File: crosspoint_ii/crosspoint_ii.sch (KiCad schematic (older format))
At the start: 1 part, among them P1 DIN_41612_128P

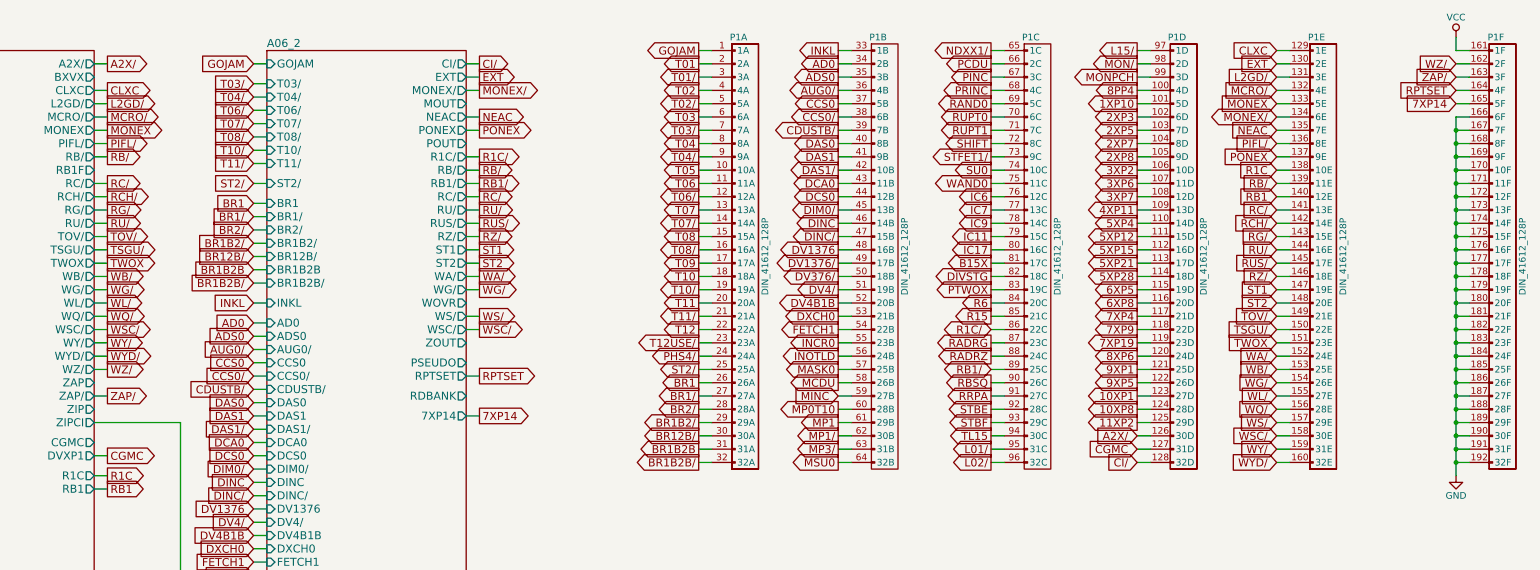
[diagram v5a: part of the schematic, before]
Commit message: Added the final four bit module. All 16 bits of the central/special registers are present. We're stuck at address 0 because TC is using RAD, which needs to be translated into RG or RZ by module 12
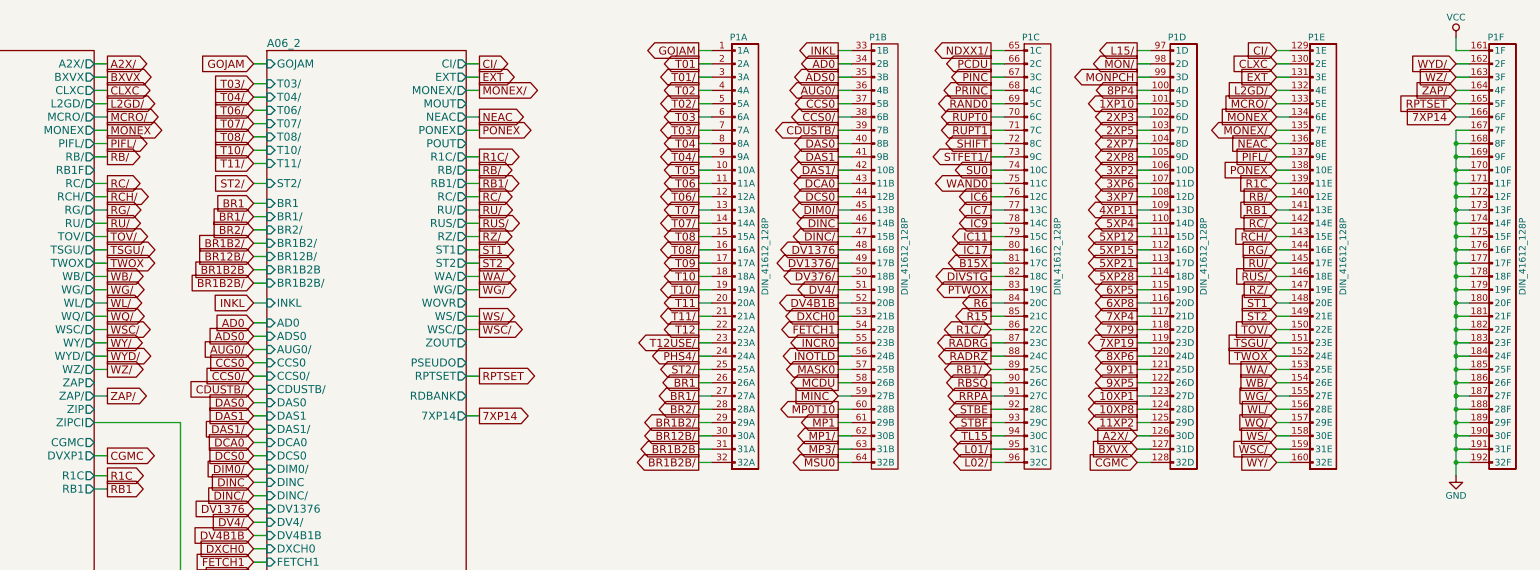
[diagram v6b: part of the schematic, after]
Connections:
- net 7XP14: now also P1.166 (6F); no longer P1.165 (5F)
- net CGMC: now also P1.128 (32D); no longer P1.127 (31D)
- net CI/: now also P1.129 (1E); no longer P1.128 (32D)
- net CLXC: now also P1.130 (2E); no longer P1.129 (1E)
- net EXT: now also P1.131 (3E); no longer P1.130 (2E)
- net GND: no longer P1.166 (6F)
- net L2GD/: now also P1.132 (4E); no longer P1.131 (3E)
- net MCRO/: now also P1.133 (5E); no longer P1.132 (4E)
- net MONEX: now also P1.134 (6E); no longer P1.133 (5E)
- net MONEX/: now also P1.135 (7E); no longer P1.134 (6E)
- net NEAC: now also P1.136 (8E); no longer P1.135 (7E)
- net PIFL/: now also P1.137 (9E); no longer P1.136 (8E)
- net PONEX: now also P1.138 (10E); no longer P1.137 (9E)
- net R1C: now also P1.139 (11E); no longer P1.138 (10E)
- net RB/: now also P1.140 (12E); no longer P1.139 (11E)
- net RB1: now also P1.141 (13E); no longer P1.140 (12E)
- net RC/: now also P1.142 (14E); no longer P1.141 (13E)
- net RCH/: now also P1.143 (15E); no longer P1.142 (14E)
- net RG/: now also P1.144 (16E); no longer P1.143 (15E)
- net RPTSET: now also P1.165 (5F); no longer P1.164 (4F)
- net RU/: now also P1.145 (17E); no longer P1.144 (16E)
- net RUS/: now also P1.146 (18E); no longer P1.145 (17E)
- net RZ/: now also P1.147 (19E); no longer P1.146 (18E)
- net ST1: now also P1.148 (20E); no longer P1.147 (19E)
- net ST2: now also P1.149 (21E); no longer P1.148 (20E)
- net TOV/: now also P1.150 (22E); no longer P1.149 (21E)
- net TSGU/: now also P1.151 (23E); no longer P1.150 (22E)
- net TWOX: now also P1.152 (24E); no longer P1.151 (23E)
- net WA/: now also P1.153 (25E); no longer P1.152 (24E)
- net WB/: now also P1.154 (26E); no longer P1.153 (25E)
- net WG/: now also P1.155 (27E); no longer P1.154 (26E)
- net WL/: now also P1.156 (28E); no longer P1.155 (27E)
- net WQ/: now also P1.157 (29E); no longer P1.156 (28E)
- net WS/: now also P1.158 (30E); no longer P1.157 (29E)
- net WSC/: now also P1.159 (31E); no longer P1.158 (30E)
- net WY/: now also P1.160 (32E); no longer P1.159 (31E)
- net WYD/: now also P1.162 (2F); no longer P1.160 (32E)
- net WZ/: now also P1.163 (3F); no longer P1.162 (2F)
- net ZAP/: now also P1.164 (4F); no longer P1.163 (3F)
- new net BXVX: P1.127 (31D)
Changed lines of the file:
@@
 Wire Wire Line
 	13150 5250 13250 5250
-Text GLabel 14200 2550 0    60   Input ~ 0
+Text GLabel 14200 2650 0    60   Input ~ 0
 EXT
 Wire Wire Line
-	14200 2550 14300 2550
+	14200 2650 14300 2650
 Text GLabel 8200 2650 2    60   Output ~ 0
 EXT
@@
 Wire Wire Line
 	8200 2750 8100 2750
-Text GLabel 14200 2950 0    60   BiDi ~ 0
+Text GLabel 14200 3050 0    60   BiDi ~ 0
 MONEX/
 Wire Wire Line
-	14200 2950 14300 2950
+	14200 3050 14300 3050
 Text GLabel 8200 3950 2    60   Output ~ 0
 ST1
@@
 Wire Wire Line
 	8200 4050 8100 4050
-Text GLabel 14200 4250 0    60   Input ~ 0
+Text GLabel 14200 4350 0    60   Input ~ 0
 ST1
 Wire Wire Line
-	14200 4250 14300 4250
-Text GLabel 14200 4350 0    60   Input ~ 0
+	14200 4350 14300 4350
+Text GLabel 14200 4450 0    60   Input ~ 0
 ST2
 Wire Wire Line
-	14200 4350 14300 4350
+	14200 4450 14300 4450
 Text GLabel 5400 3950 2    60   Output ~ 0
 TSGU/
 Wire Wire Line
 	5400 3950 5300 3950
-Text GLabel 14200 4550 0    60   Input ~ 0
+Text GLabel 14200 4650 0    60   Input ~ 0
 TSGU/
 Wire Wire Line
-	14200 4550 14300 4550
+	14200 4650 14300 4650
 Text GLabel 3650 7000 0    60   Input ~ 0
 3XP7
@@
 Wire Wire Line
 	8200 5200 8100 5200
-Text GLabel 15550 2850 0    60   Input ~ 0
+Text GLabel 15550 2950 0    60   Input ~ 0
 7XP14
 Wire Wire Line
-	15550 2850 15650 2850
+	15550 2950 15650 2950
 Text GLabel 8200 4900 2    60   Output ~ 0
 RPTSET
 Wire Wire Line
 	8200 4900 8100 4900
-Text GLabel 15550 2750 0    60   Input ~ 0
+Text GLabel 15550 2850 0    60   Input ~ 0
 RPTSET
 Wire Wire Line
-	15550 2750 15650 2750
+	15550 2850 15650 2850
 Text GLabel 5400 3850 2    60   Output ~ 0
 TOV/
 Wire Wire Line
 	5400 3850 5300 3850
-Text GLabel 14200 4450 0    60   Input ~ 0
+Text GLabel 14200 4550 0    60   Input ~ 0
 TOV/
 Wire Wire Line
-	14200 4450 14300 4450
+	14200 4550 14300 4550
 Text GLabel 5400 2550 2    60   Output ~ 0
 A2X/
@@
 Wire Wire Line
 	5400 5500 5300 5500
-Text GLabel 13150 5450 0    60   Input ~ 0
+Text GLabel 13150 5550 0    60   Input ~ 0
 CGMC
 Wire Wire Line
-	13150 5450 13250 5450
+	13150 5550 13250 5550
 Text GLabel 8200 2550 2    60   Output ~ 0
 CI/
 Wire Wire Line
 	8200 2550 8100 2550
-Text GLabel 13150 5550 0    60   Input ~ 0
+Text GLabel 14200 2450 0    60   Input ~ 0
 CI/
 Wire Wire Line
-	13150 5550 13250 5550
+	14200 2450 14300 2450
 Text GLabel 5400 2850 2    60   Output ~ 0
 L2GD/
 Wire Wire Line
 	5400 2850 5300 2850
-Text GLabel 14200 2650 0    60   Input ~ 0
+Text GLabel 14200 2750 0    60   Input ~ 0
 L2GD/
 Wire Wire Line
-	14200 2650 14300 2650
+	14200 2750 14300 2750
 Text GLabel 8200 2950 2    60   Output ~ 0
 NEAC
 Wire Wire Line
 	8200 2950 8100 2950
-Text GLabel 14200 3050 0    60   Input ~ 0
+Text GLabel 14200 3150 0    60   Input ~ 0
 NEAC
 Wire Wire Line
-	14200 3050 14300 3050
+	14200 3150 14300 3150
 Text GLabel 5400 3150 2    60   Output ~ 0
 PIFL/
 Wire Wire Line
 	5400 3150 5300 3150
-Text GLabel 14200 3150 0    60   Input ~ 0
+Text GLabel 14200 3250 0    60   Input ~ 0
 PIFL/
 Wire Wire Line
-	14200 3150 14300 3150
+	14200 3250 14300 3250
 Text GLabel 5400 3250 2    60   Output ~ 0
 RB/
@@
 Wire Wire Line
 	8200 3350 8100 3350
-Text GLabel 14200 3450 0    60   Input ~ 0
+Text GLabel 14200 3550 0    60   Input ~ 0
 RB/
 Wire Wire Line
-	14200 3450 14300 3450
+	14200 3550 14300 3550
 Text GLabel 5400 3550 2    60   Output ~ 0
 RCH/
 Wire Wire Line
 	5400 3550 5300 3550
-Text GLabel 14200 3750 0    60   Input ~ 0
+Text GLabel 14200 3850 0    60   Input ~ 0
 RCH/
 Wire Wire Line
-	14200 3750 14300 3750
+	14200 3850 14300 3850
 Text GLabel 5400 3450 2    60   Output ~ 0
 RC/
@@
 Wire Wire Line
 	8200 3550 8100 3550
-Text GLabel 14200 3650 0    60   Input ~ 0
+Text GLabel 14200 3750 0    60   Input ~ 0
 RC/
 Wire Wire Line
-	14200 3650 14300 3650
+	14200 3750 14300 3750
 Text GLabel 5400 3650 2    60   Output ~ 0
 RG/
 Wire Wire Line
 	5400 3650 5300 3650
-Text GLabel 14200 3850 0    60   Input ~ 0
+Text GLabel 14200 3950 0    60   Input ~ 0
 RG/
 Wire Wire Line
-	14200 3850 14300 3850
+	14200 3950 14300 3950
 $Comp
 L DIN_41612_128P P1
@@
 Connection ~ 15550 3150
 Wire Wire Line
-	15550 2950 15650 2950
-Connection ~ 15550 3050
-Wire Wire Line
 	15550 3650 15650 3650
 Wire Wire Line
@@
 Connection ~ 15550 3650
 Connection ~ 15550 3550
-Wire Wire Line
-	15550 2950 15550 5650
 Text GLabel 8200 3750 2    60   Output ~ 0
 RUS/
 Wire Wire Line
 	8200 3750 8100 3750
-Text GLabel 14200 3950 0    60   Input ~ 0
+Text GLabel 14200 4050 0    60   Input ~ 0
 RU/
 Wire Wire Line
-	14200 3950 14300 3950
+	14200 4050 14300 4050
 Text GLabel 5400 3750 2    60   Output ~ 0
 RU/
@@
 Wire Wire Line
 	8200 3650 8100 3650
-Text GLabel 14200 4050 0    60   Input ~ 0
+Text GLabel 14200 4150 0    60   Input ~ 0
 RUS/
 Wire Wire Line
-	14200 4050 14300 4050
+	14200 4150 14300 4150
 Text GLabel 8200 3850 2    60   Output ~ 0
 RZ/
 Wire Wire Line
 	8200 3850 8100 3850
-Text GLabel 14200 4150 0    60   Input ~ 0
+Text GLabel 14200 4250 0    60   Input ~ 0
 RZ/
 Wire Wire Line
-	14200 4150 14300 4150
+	14200 4250 14300 4250
 Text GLabel 8200 4150 2    60   Output ~ 0
 WA/
 Wire Wire Line
 	8200 4150 8100 4150
-Text GLabel 14200 4750 0    60   Input ~ 0
+Text GLabel 14200 4850 0    60   Input ~ 0
 WA/
 Wire Wire Line
-	14200 4750 14300 4750
+	14200 4850 14300 4850
 Text GLabel 5400 4150 2    60   Output ~ 0
 WB/
 Wire Wire Line
 	5400 4150 5300 4150
-Text GLabel 14200 4850 0    60   Input ~ 0
+Text GLabel 14200 4950 0    60   Input ~ 0
 WB/
 Wire Wire Line
-	14200 4850 14300 4850
+	14200 4950 14300 4950
 Text GLabel 5400 4250 2    60   Output ~ 0
 WG/
@@
 Wire Wire Line
 	8200 4250 8100 4250
-Text GLabel 14200 4950 0    60   Input ~ 0
+Text GLabel 14200 5050 0    60   Input ~ 0
 WG/
 Wire Wire Line
-	14200 4950 14300 4950
+	14200 5050 14300 5050
 Text GLabel 5400 4350 2    60   Output ~ 0
 WL/
 Wire Wire Line
 	5400 4350 5300 4350
-Text GLabel 14200 5050 0    60   Input ~ 0
+Text GLabel 14200 5150 0    60   Input ~ 0
 WL/
 Wire Wire Line
-	14200 5050 14300 5050
+	14200 5150 14300 5150
 Text GLabel 5400 4450 2    60   Output ~ 0
 WQ/
 Wire Wire Line
 	5400 4450 5300 4450
-Text GLabel 14200 5150 0    60   Input ~ 0
+Text GLabel 14200 5250 0    60   Input ~ 0
 WQ/
 Wire Wire Line
-	14200 5150 14300 5150
+	14200 5250 14300 5250
 Text GLabel 5400 4550 2    60   Output ~ 0
 WSC/
@@
 Wire Wire Line
 	8200 4550 8100 4550
-Text GLabel 14200 5350 0    60   Input ~ 0
+Text GLabel 14200 5450 0    60   Input ~ 0
 WSC/
 Wire Wire Line
-	14200 5350 14300 5350
+	14200 5450 14300 5450
 Text GLabel 8200 4450 2    60   Output ~ 0
 WS/
 Wire Wire Line
 	8200 4450 8100 4450
-Text GLabel 14200 5250 0    60   Input ~ 0
+Text GLabel 14200 5350 0    60   Input ~ 0
 WS/
 Wire Wire Line
-	14200 5250 14300 5250
+	14200 5350 14300 5350
 Text GLabel 5400 4750 2    60   Output ~ 0
 WYD/
 Wire Wire Line
 	5400 4750 5300 4750
-Text GLabel 14200 5550 0    60   Input ~ 0
+Text GLabel 15550 2550 0    60   Input ~ 0
 WYD/
 Wire Wire Line
-	14200 5550 14300 5550
+	15550 2550 15650 2550
 Text GLabel 5400 4650 2    60   Output ~ 0
 WY/
 Wire Wire Line
 	5400 4650 5300 4650
-Text GLabel 14200 5450 0    60   Input ~ 0
+Text GLabel 14200 5550 0    60   Input ~ 0
 WY/
 Wire Wire Line
-	14200 5450 14300 5450
+	14200 5550 14300 5550
 Text GLabel 5400 4850 2    60   Output ~ 0
 WZ/
 Wire Wire Line
 	5400 4850 5300 4850
-Text GLabel 15550 2550 0    60   Input ~ 0
+Text GLabel 15550 2650 0    60   Input ~ 0
 WZ/
 Wire Wire Line
-	15550 2550 15650 2550
+	15550 2650 15650 2650
 Text GLabel 5400 5050 2    60   Output ~ 0
 ZAP/
 Wire Wire Line
 	5400 5050 5300 5050
-Text GLabel 15550 2650 0    60   Input ~ 0
+Text GLabel 15550 2750 0    60   Input ~ 0
 ZAP/
 Wire Wire Line
-	15550 2650 15650 2650
+	15550 2750 15650 2750
 Text GLabel 5400 2750 2    60   Output ~ 0
 CLXC
 Wire Wire Line
 	5400 2750 5300 2750
-Text GLabel 14200 2450 0    60   Input ~ 0
+Text GLabel 14200 2550 0    60   Input ~ 0
 CLXC
 Wire Wire Line
-	14200 2450 14300 2450
+	14200 2550 14300 2550
 Text GLabel 5400 2950 2    60   Output ~ 0
 MCRO/
 Wire Wire Line
 	5400 2950 5300 2950
-Text GLabel 14200 2750 0    60   Input ~ 0
+Text GLabel 14200 2850 0    60   Input ~ 0
 MCRO/
 Wire Wire Line
-	14200 2750 14300 2750
+	14200 2850 14300 2850
 Text GLabel 8200 3050 2    60   Output ~ 0
 PONEX
 Wire Wire Line
 	8200 3050 8100 3050
-Text GLabel 14200 3250 0    60   Input ~ 0
+Text GLabel 14200 3350 0    60   Input ~ 0
 PONEX
 Wire Wire Line
-	14200 3250 14300 3250
+	14200 3350 14300 3350
 Text GLabel 8200 3250 2    60   Output ~ 0
 R1C/
@@
 Wire Wire Line
 	12050 4550 12150 4550
-Text GLabel 14200 3550 0    60   Input ~ 0
+Text GLabel 14200 3650 0    60   Input ~ 0
 RB1
 Wire Wire Line
-	14200 3550 14300 3550
-Text GLabel 14200 3350 0    60   Input ~ 0
+	14200 3650 14300 3650
+Text GLabel 14200 3450 0    60   Input ~ 0
 R1C
 Wire Wire Line
-	14200 3350 14300 3350
+	14200 3450 14300 3450
 Text GLabel 5400 4050 2    60   Output ~ 0
 TWOX
 Wire Wire Line
 	5400 4050 5300 4050
-Text GLabel 14200 4650 0    60   Input ~ 0
+Text GLabel 14200 4750 0    60   Input ~ 0
 TWOX
 Wire Wire Line
-	14200 4650 14300 4650
+	14200 4750 14300 4750
 Text GLabel 5400 3050 2    60   Output ~ 0
 MONEX
 Wire Wire Line
 	5400 3050 5300 3050
-Text GLabel 14200 2850 0    60   Input ~ 0
+Text GLabel 14200 2950 0    60   Input ~ 0
 MONEX
 Wire Wire Line
-	14200 2850 14300 2850
+	14200 2950 14300 2950
+Text GLabel 5400 2650 2    60   Output ~ 0
+BXVX
+Wire Wire Line
+	5400 2650 5300 2650
+Wire Wire Line
+	15550 3050 15550 5650
+Text GLabel 13150 5450 0    60   Input ~ 0
+BXVX
+Wire Wire Line
+	13150 5450 13250 5450
 $EndSCHEMATC

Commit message: Added in WHOMP, whatever it is
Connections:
- net 10XP1: now also P1.124 (28D); no longer P1.123 (27D)
- net 10XP8: now also P1.125 (29D); no longer P1.124 (28D)
- net 11XP2: now also P1.126 (30D); no longer P1.125 (29D)
- net 1XP10: now also P1.102 (6D); no longer P1.101 (5D)
- net 2XP3: now also P1.103 (7D); no longer P1.102 (6D)
- net 2XP5: now also P1.104 (8D); no longer P1.103 (7D)
- net 2XP7: now also P1.105 (9D); no longer P1.104 (8D)
- net 2XP8: now also P1.106 (10D); no longer P1.105 (9D)
- net 3XP2: now also P1.107 (11D); no longer P1.106 (10D)
- net 3XP6: now also P1.108 (12D); no longer P1.107 (11D)
- net 3XP7: now also P1.109 (13D); no longer P1.108 (12D)
- net 4XP11: now also P1.110 (14D); no longer P1.109 (13D)
- net 5XP12: now also P1.112 (16D); no longer P1.111 (15D)
- net 5XP15: now also P1.113 (17D); no longer P1.112 (16D)
- net 5XP21: now also P1.114 (18D); no longer P1.113 (17D)
- net 5XP28: now also P1.115 (19D); no longer P1.114 (18D)
- net 5XP4: now also P1.111 (15D); no longer P1.110 (14D)
- net 6XP5: now also P1.116 (20D); no longer P1.115 (19D)
- net 6XP8: now also P1.117 (21D); no longer P1.116 (20D)
- net 7XP14: now also P1.167 (7F); no longer P1.166 (6F)
- net 7XP19: now also P1.120 (24D); no longer P1.119 (23D)
- net 7XP4: now also P1.118 (22D); no longer P1.117 (21D)
- net 7XP9: now also P1.119 (23D); no longer P1.118 (22D)
- net 8PP4: now also P1.101 (5D); no longer P1.100 (4D)
- net 8XP6: now also P1.121 (25D); no longer P1.120 (24D)
- net 9XP1: now also P1.122 (26D); no longer P1.121 (25D)
- net 9XP5: now also P1.123 (27D); no longer P1.122 (26D)
- net A2X/: now also P1.127 (31D); no longer P1.126 (30D)
- net B15X: now also P1.82 (18C); no longer P1.81 (17C)
- net BXVX: now also P1.128 (32D); no longer P1.127 (31D)
- net CGMC: now also P1.129 (1E); no longer P1.128 (32D)
- net CI/: now also P1.130 (2E); no longer P1.129 (1E)
- net CLXC: now also P1.131 (3E); no longer P1.130 (2E)
- net DIVSTG: now also P1.83 (19C); no longer P1.82 (18C)
- net EXT: now also P1.132 (4E); no longer P1.131 (3E)
- net GND: no longer P1.167 (7F), P1.168 (8F), P1.169 (9F)
- net IC11: now also P1.80 (16C); no longer P1.79 (15C)
- net IC17: now also P1.81 (17C); no longer P1.80 (16C)
- net IC6: now also P1.77 (13C); no longer P1.76 (12C)
- net IC7: now also P1.78 (14C); no longer P1.77 (13C)
- net IC9: now also P1.79 (15C); no longer P1.78 (14C)
- net L01/: now also P1.96 (32C); no longer P1.95 (31C)
- net L02/: now also P1.97 (1D); no longer P1.96 (32C)
- net L15/: now also P1.98 (2D); no longer P1.97 (1D)
- net L2GD/: now also P1.133 (5E); no longer P1.132 (4E)
- net MCRO/: now also P1.134 (6E); no longer P1.133 (5E)
- net MON/: now also P1.99 (3D); no longer P1.98 (2D)
- net MONEX: now also P1.135 (7E); no longer P1.134 (6E)
- net MONEX/: now also P1.136 (8E); no longer P1.135 (7E)
- net MONPCH: now also P1.100 (4D); no longer P1.99 (3D)
- net NEAC: now also P1.137 (9E); no longer P1.136 (8E)
- net PCDU: now also P1.67 (3C); no longer P1.66 (2C)
- net PIFL/: now also P1.138 (10E); no longer P1.137 (9E)
- net PINC: now also P1.68 (4C); no longer P1.67 (3C)
- net PONEX: now also P1.139 (11E); no longer P1.138 (10E)
- net PRINC: now also P1.69 (5C); no longer P1.68 (4C)
- net PTWOX: now also P1.84 (20C); no longer P1.83 (19C)
- net R15: now also P1.86 (22C); no longer P1.85 (21C)
- net R1C: now also P1.140 (12E); no longer P1.139 (11E)
- net R1C/: now also P1.87 (23C); no longer P1.86 (22C)
- net R6: now also P1.85 (21C); no longer P1.84 (20C)
- net RADRG: now also P1.88 (24C); no longer P1.87 (23C)
- net RADRZ: now also P1.89 (25C); no longer P1.88 (24C)
- net RAND0: now also P1.70 (6C); no longer P1.69 (5C)
- net RB/: now also P1.141 (13E); no longer P1.140 (12E)
- net RB1: now also P1.142 (14E); no longer P1.141 (13E)
- net RB1/: now also P1.90 (26C); no longer P1.89 (25C)
- net RBSQ: now also P1.91 (27C); no longer P1.90 (26C)
- net RC/: now also P1.143 (15E); no longer P1.142 (14E)
- net RCH/: now also P1.144 (16E); no longer P1.143 (15E)
- net RG/: now also P1.145 (17E); no longer P1.144 (16E)
- net RPTSET: now also P1.166 (6F); no longer P1.165 (5F)
- net RRPA: now also P1.92 (28C); no longer P1.91 (27C)
- net RU/: now also P1.146 (18E); no longer P1.145 (17E)
- net RUPT0: now also P1.71 (7C); no longer P1.70 (6C)
- net RUPT1: now also P1.72 (8C); no longer P1.71 (7C)
- net RUS/: now also P1.147 (19E); no longer P1.146 (18E)
- net RZ/: now also P1.148 (20E); no longer P1.147 (19E)
- net SHIFT: now also P1.73 (9C); no longer P1.72 (8C)
- net ST1: now also P1.149 (21E); no longer P1.148 (20E)
- net ST2: now also P1.150 (22E); no longer P1.149 (21E)
- net STBE: now also P1.93 (29C); no longer P1.92 (28C)
- net STBF: now also P1.94 (30C); no longer P1.93 (29C)
- net STFET1/: now also P1.74 (10C); no longer P1.73 (9C)
- net SU0: now also P1.75 (11C); no longer P1.74 (10C)
- net TL15: now also P1.95 (31C); no longer P1.94 (30C)
- net TOV/: now also P1.151 (23E); no longer P1.150 (22E)
- net TSGU/: now also P1.152 (24E); no longer P1.151 (23E)
- net TWOX: now also P1.153 (25E); no longer P1.152 (24E)
- net WA/: now also P1.154 (26E); no longer P1.153 (25E)
- net WAND0: now also P1.76 (12C); no longer P1.75 (11C)
- net WB/: now also P1.155 (27E); no longer P1.154 (26E)
- net WG/: now also P1.156 (28E); no longer P1.155 (27E)
- net WL/: now also P1.157 (29E); no longer P1.156 (28E)
- net WQ/: now also P1.158 (30E); no longer P1.157 (29E)
- net WS/: now also P1.159 (31E); no longer P1.158 (30E)
- net WSC/: now also P1.160 (32E); no longer P1.159 (31E)
- net WY/: now also P1.162 (2F); no longer P1.160 (32E)
- net WYD/: now also P1.163 (3F); no longer P1.162 (2F)
- net WZ/: now also P1.164 (4F); no longer P1.163 (3F)
- net ZAP/: now also P1.165 (5F); no longer P1.164 (4F)
- new net NISQ: P1.66 (2C)
- new net WHOMP: P1.168 (8F)
- new net WHOMPA: P1.169 (9F)
